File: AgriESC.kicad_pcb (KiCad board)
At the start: 2 copper layers, 94.5 x 53.5 mm, 309 parts, among them J1 SUPPLY, J10 GPIO, J11 USB_OTG, J12 HALL_ENC, J2 PH_A, J3 PH_B, J4 PH_C, J6 COMM, J7 SERVO, J8 CAN, J9 SWD, SW1 SW_SPDT, U1 FDMS7698, U10 STM32F405RGT6, U11 DRV8303, U12 TJA1051TK-3, U13 LMR16006YQ, U14 MCP1700-3302E_SOT23, U15 MCP1700-3302E_SOT23, U2 FDMS7698, U3 FDMS7698, U4 FDMS7698, U5 FDMS7698, U6 FDMS7698, U7 MAX9920, U8 MAX9920, U9 MAX9920, Y1 8M Resonator

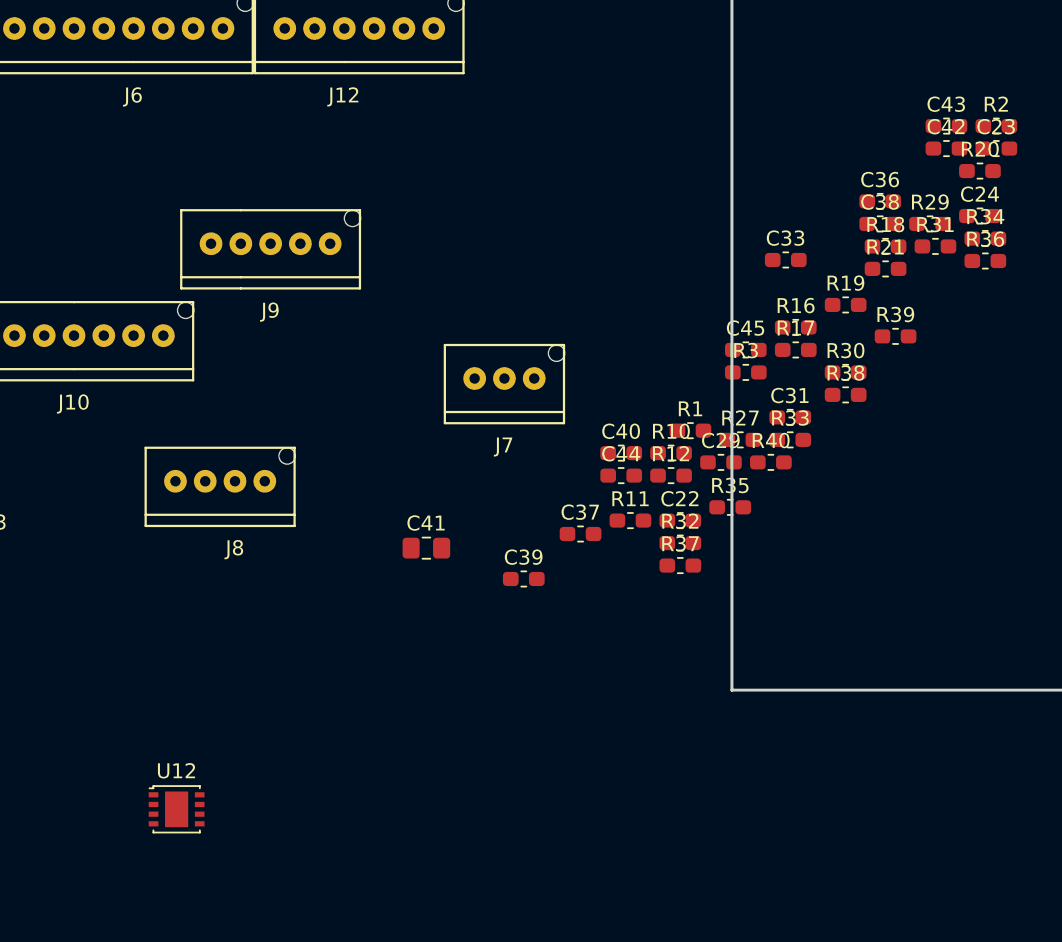
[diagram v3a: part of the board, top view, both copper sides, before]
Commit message: Added CAN wiring
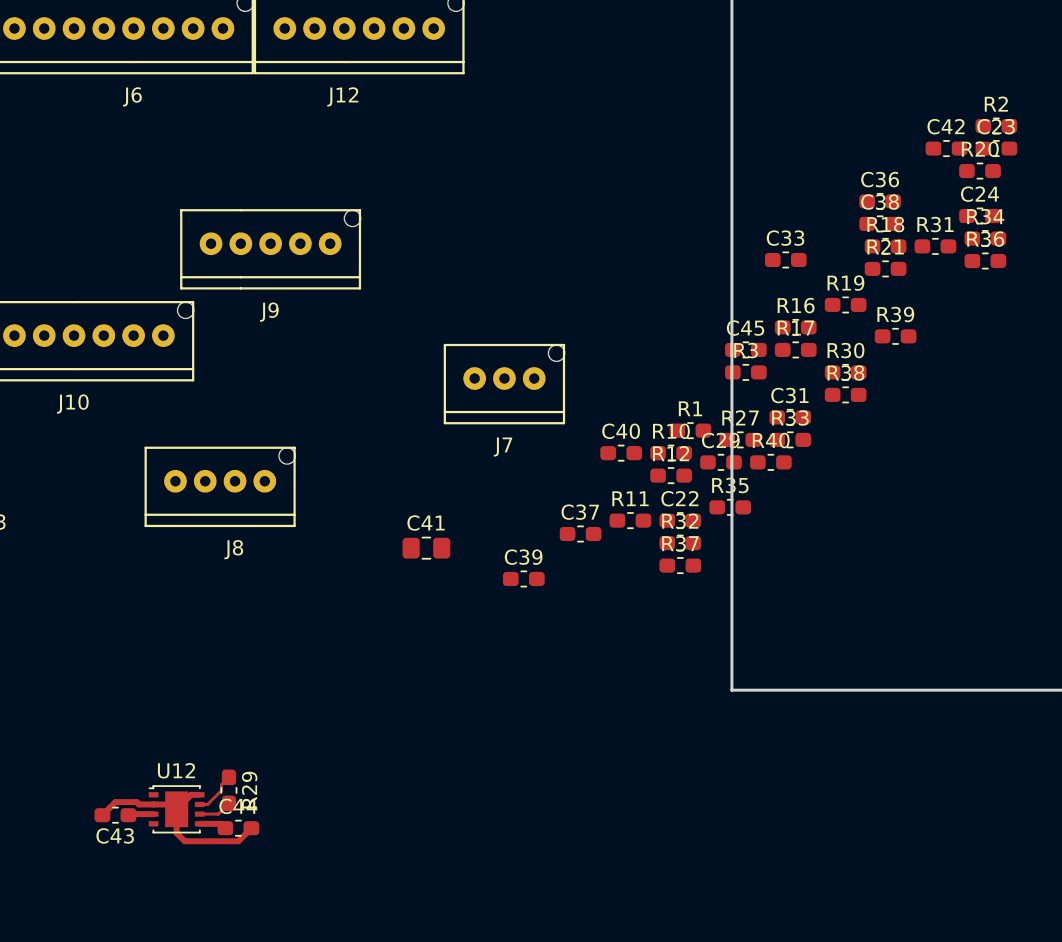
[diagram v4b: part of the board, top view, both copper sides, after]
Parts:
- moved C43 72.5 mm to (14.6, 63.9), turned to 180 degrees
- moved R29 60.5 mm to (22.2, 62.2), turned to 270 degrees
- moved C44 34.9 mm to (22.9, 64.8)
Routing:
- net SL_A: track 198.0 -> 212.7 mm
- net CANH: track 0.00 -> 2.94 mm
- net CANL: track 0.00 -> 2.26 mm
- net VCC: track 2.21 -> 4.05 mm
- net +5V: track 29.0 -> 30.7 mm
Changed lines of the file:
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@@
     (thickness 1.6)
     (drawings 4)
-    (tracks 373)
+    (tracks 396)
     (zones 0)
     (modules 309)
@@
   )
   (setup
-    (last_trace_width 0.2)
+    (last_trace_width 0.4)
     (user_trace_width 0.2)
     (user_trace_width 0.3)
@@
   )
   (module Capacitor_SMD:C_0603_1608Metric_Pad1.05x0.95mm_HandSolder (layer F.Cu)
-    (at 70.405001 17.625001)
+    (at 14.605 63.895 180)
     (descr "Capacitor SMD 0603 (1608 Metric), square (rectangular) end terminal, IPC_7351 nominal with elongated pad for handsoldering. (Body size source: http://www.tortai-tech.com/upload/download/2011102023233369053.pdf), generated with kicad-footprint-generator")
     (tags "capacitor handsolder")
     (attr smd)
-    (fp_text reference C43 (at 0 -1.43) (layer F.SilkS)
+    (fp_text reference C43 (at 0 -1.43 180) (layer F.SilkS)
       (effects (font (size 1 1) (thickness 0.15)))
     )
-    (fp_text value 2u2_5V (at 0 1.43) (layer F.Fab)
+    (fp_text value 2u2_5V (at 0 1.43 180) (layer F.Fab)
       (effects (font (size 1 1) (thickness 0.15)))
     )
@@
     (fp_line (start 1.65 -0.73) (end 1.65 0.73) (layer F.CrtYd) (width 0.05))
     (fp_line (start 1.65 0.73) (end -1.65 0.73) (layer F.CrtYd) (width 0.05))
-    (fp_text user %R (at 0 0) (layer F.Fab)
+    (fp_text user %R (at 0 0 180) (layer F.Fab)
       (effects (font (size 0.4 0.4) (thickness 0.06)))
     )
-    (pad 1 smd roundrect (at -0.875 0) (size 1.05 0.95) (layers F.Cu F.Paste F.Mask) (roundrect_rratio 0.25)
+    (pad 1 smd roundrect (at -0.875 0 180) (size 1.05 0.95) (layers F.Cu F.Paste F.Mask) (roundrect_rratio 0.25)
       (net 23 +5V))
-    (pad 2 smd roundrect (at 0.875 0) (size 1.05 0.95) (layers F.Cu F.Paste F.Mask) (roundrect_rratio 0.25)
+    (pad 2 smd roundrect (at 0.875 0 180) (size 1.05 0.95) (layers F.Cu F.Paste F.Mask) (roundrect_rratio 0.25)
       (net 1 SL_A))
     (model ${KISYS3DMOD}/Capacitor_SMD.3dshapes/C_0603_1608Metric.wrl
@@
   )
   (module Capacitor_SMD:C_0603_1608Metric_Pad1.05x0.95mm_HandSolder (layer F.Cu)
-    (at 48.565001 41.095001)
+    (at 22.86 64.77)
     (descr "Capacitor SMD 0603 (1608 Metric), square (rectangular) end terminal, IPC_7351 nominal with elongated pad for handsoldering. (Body size source: http://www.tortai-tech.com/upload/download/2011102023233369053.pdf), generated with kicad-footprint-generator")
     (tags "capacitor handsolder")
@@
   )
   (module Resistor_SMD:R_0603_1608Metric_Pad1.05x0.95mm_HandSolder (layer F.Cu)
-    (at 69.305001 24.195001)
+    (at 22.225 62.23 270)
     (descr "Resistor SMD 0603 (1608 Metric), square (rectangular) end terminal, IPC_7351 nominal with elongated pad for handsoldering. (Body size source: http://www.tortai-tech.com/upload/download/2011102023233369053.pdf), generated with kicad-footprint-generator")
     (tags "resistor handsolder")
     (attr smd)
-    (fp_text reference R29 (at 0 -1.43) (layer F.SilkS)
+    (fp_text reference R29 (at 0 -1.43 270) (layer F.SilkS)
       (effects (font (size 1 1) (thickness 0.15)))
     )
-    (fp_text value 220R (at 0 1.43) (layer F.Fab)
+    (fp_text value 220R (at 0 1.43 270) (layer F.Fab)
       (effects (font (size 1 1) (thickness 0.15)))
     )
-    (fp_text user %R (at 0 0) (layer F.Fab)
+    (fp_text user %R (at 0 0 270) (layer F.Fab)
       (effects (font (size 0.4 0.4) (thickness 0.06)))
     )
@@
     (fp_line (start -0.8 -0.4) (end 0.8 -0.4) (layer F.Fab) (width 0.1))
     (fp_line (start -0.8 0.4) (end -0.8 -0.4) (layer F.Fab) (width 0.1))
-    (pad 2 smd roundrect (at 0.875 0) (size 1.05 0.95) (layers F.Cu F.Paste F.Mask) (roundrect_rratio 0.25)
+    (pad 2 smd roundrect (at 0.875 0 270) (size 1.05 0.95) (layers F.Cu F.Paste F.Mask) (roundrect_rratio 0.25)
       (net 42 CANL))
-    (pad 1 smd roundrect (at -0.875 0) (size 1.05 0.95) (layers F.Cu F.Paste F.Mask) (roundrect_rratio 0.25)
+    (pad 1 smd roundrect (at -0.875 0 270) (size 1.05 0.95) (layers F.Cu F.Paste F.Mask) (roundrect_rratio 0.25)
       (net 41 CANH))
     (model ${KISYS3DMOD}/Resistor_SMD.3dshapes/R_0603_1608Metric.wrl
@@
   (segment (start 55.245 91.44) (end 58.42 94.615) (width 0.2) (layer B.Cu) (net 1))
   (segment (start 55.245 87.63) (end 55.245 91.44) (width 0.2) (layer B.Cu) (net 1))
+  (segment (start 19.690001 62.525) (end 18.715001 63.5) (width 0.4) (layer F.Cu) (net 1))
+  (segment (start 20.265001 62.525) (end 19.690001 62.525) (width 0.4) (layer F.Cu) (net 1))
+  (segment (start 18.390001 63.175) (end 18.715001 63.5) (width 0.4) (layer F.Cu) (net 1))
+  (segment (start 17.165001 63.175) (end 18.390001 63.175) (width 0.4) (layer F.Cu) (net 1))
+  (segment (start 14.229072 63.395928) (end 13.73 63.895) (width 0.4) (layer F.Cu) (net 1))
+  (segment (start 14.60501 63.01999) (end 14.229072 63.395928) (width 0.4) (layer F.Cu) (net 1))
+  (segment (start 16.031566 63.01999) (end 14.60501 63.01999) (width 0.4) (layer F.Cu) (net 1))
+  (segment (start 16.186576 63.175) (end 16.031566 63.01999) (width 0.4) (layer F.Cu) (net 1))
+  (segment (start 17.165001 63.175) (end 16.186576 63.175) (width 0.4) (layer F.Cu) (net 1))
+  (segment (start 18.715001 65.1) (end 18.715001 63.5) (width 0.4) (layer F.Cu) (net 1))
+  (segment (start 22.85999 65.64501) (end 19.260011 65.64501) (width 0.4) (layer F.Cu) (net 1))
+  (segment (start 19.260011 65.64501) (end 18.715001 65.1) (width 0.4) (layer F.Cu) (net 1))
+  (segment (start 23.735 64.77) (end 22.85999 65.64501) (width 0.4) (layer F.Cu) (net 1))
   (segment (start 114.775 22.975) (end 114.75 23) (width 0.25) (layer F.Cu) (net 2))
   (segment (start 114.775 21) (end 114.775 22.975) (width 0.25) (layer F.Cu) (net 2))
@@
   (segment (start 58.615 -8.015) (end 58.69 -7.94) (width 0.4) (layer F.Cu) (net 4))
   (segment (start 56.515 -8.015) (end 58.615 -8.015) (width 0.4) (layer F.Cu) (net 4))
+  (segment (start 21.69 64.475) (end 21.985 64.77) (width 0.4) (layer F.Cu) (net 4))
+  (segment (start 20.265001 64.475) (end 21.69 64.475) (width 0.4) (layer F.Cu) (net 4))
   (segment (start 119.217 34.5) (end 119.25 34.5) (width 0.2) (layer F.Cu) (net 12))
   (segment (start 117.405 36.312) (end 119.217 34.5) (width 0.2) (layer F.Cu) (net 12))
@@
   (segment (start 61.99 -8.89) (end 62.865 -8.015) (width 0.4) (layer F.Cu) (net 23))
   (segment (start 60.69 -8.89) (end 61.99 -8.89) (width 0.4) (layer F.Cu) (net 23))
+  (segment (start 15.55 63.825) (end 15.48 63.895) (width 0.4) (layer F.Cu) (net 23))
+  (segment (start 17.165001 63.825) (end 15.55 63.825) (width 0.4) (layer F.Cu) (net 23))
   (segment (start 58.07 88.73) (end 59.17 87.63) (width 0.4) (layer F.Cu) (net 25))
   (segment (start 56.195 88.73) (end 58.07 88.73) (width 0.4) (layer F.Cu) (net 25))
@@
   (segment (start 145.75 39.9875) (end 146.75 40.9875) (width 0.2) (layer F.Cu) (net 34))
   (segment (start 145.75 39.75) (end 145.75 39.9875) (width 0.2) (layer F.Cu) (net 34))
+  (segment (start 21.725928 61.854072) (end 22.225 61.355) (width 0.2) (layer F.Cu) (net 41))
+  (segment (start 21.725928 62.239073) (end 21.725928 61.854072) (width 0.2) (layer F.Cu) (net 41))
+  (segment (start 20.790001 63.175) (end 21.725928 62.239073) (width 0.2) (layer F.Cu) (net 41))
+  (segment (start 20.265001 63.175) (end 20.790001 63.175) (width 0.2) (layer F.Cu) (net 41))
+  (segment (start 21.505 63.825) (end 22.225 63.105) (width 0.2) (layer F.Cu) (net 42))
+  (segment (start 20.265001 63.825) (end 21.505 63.825) (width 0.2) (layer F.Cu) (net 42))
   (segment (start 74.295 -26.275) (end 73.025 -25.005) (width 0.2) (layer F.Cu) (net 49))
   (segment (start 74.295 -27.305) (end 74.295 -26.275) (width 0.2) (layer F.Cu) (net 49))

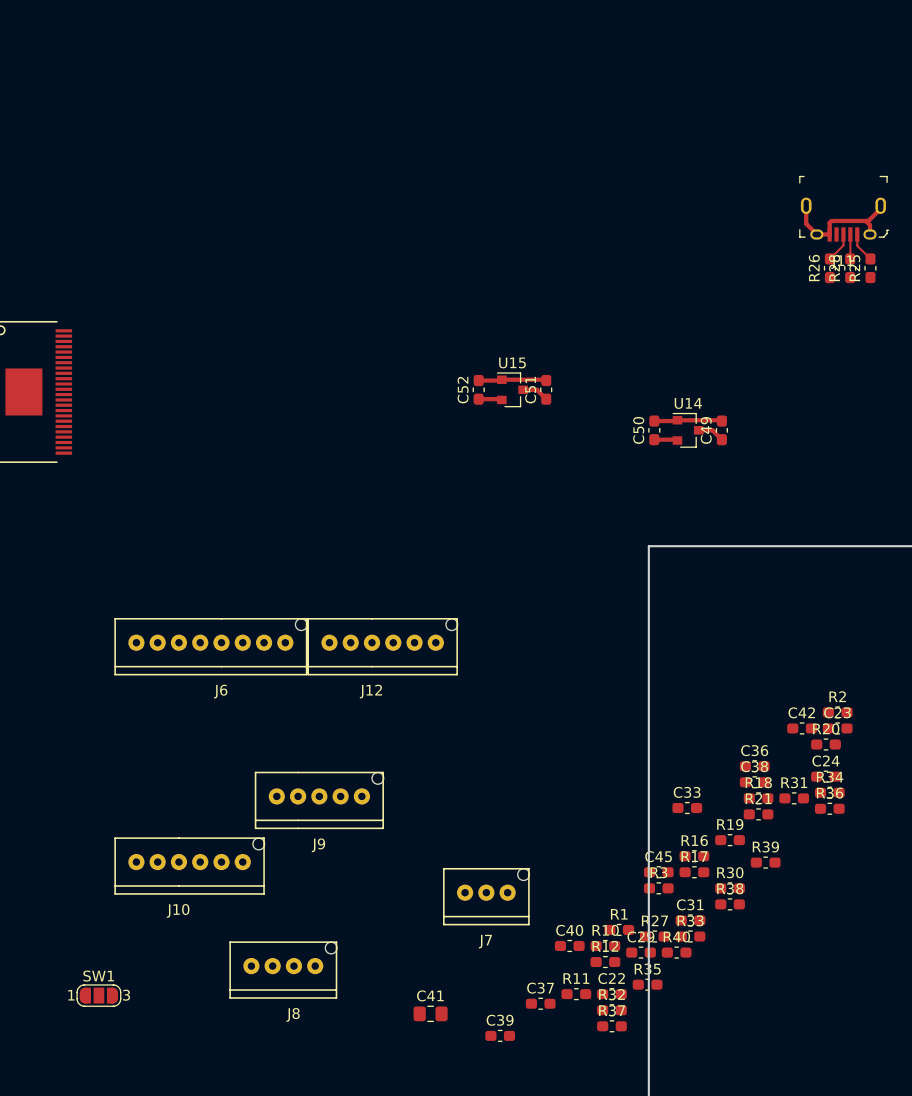
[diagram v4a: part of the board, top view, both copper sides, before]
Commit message: Arranged hall sensors
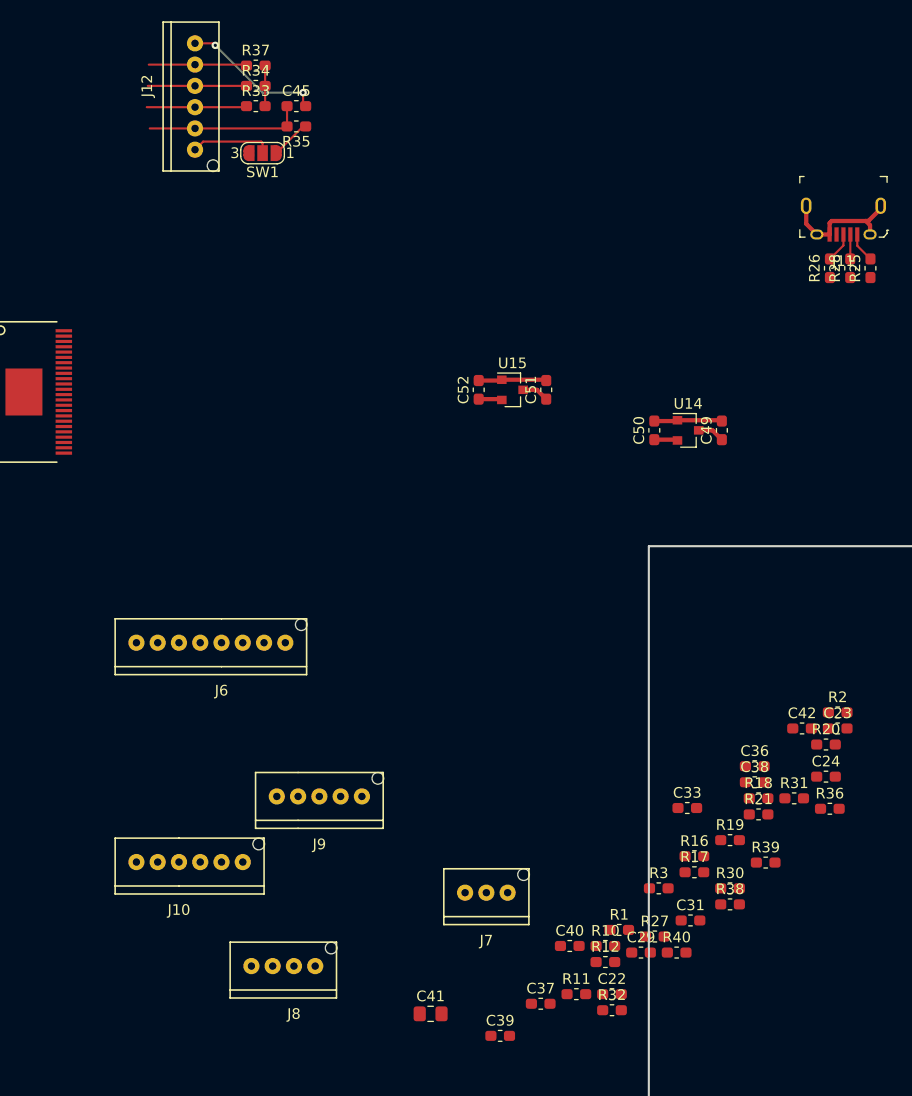
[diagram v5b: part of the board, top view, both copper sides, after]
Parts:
- moved R37 96.3 mm to (19.1, -43.2)
- moved R33 88.1 mm to (19.1, -39.4)
- moved R35 87.2 mm to (22.9, -37.5), turned to 180 degrees
- moved R34 85.6 mm to (19.1, -41.3)
- moved SW1 80.7 mm to (19.7, -35.0), turned to 180 degrees
- moved C45 79.7 mm to (22.9, -39.4)
- moved J12 54.9 mm to (13.3, -41.3), turned to 270 degrees
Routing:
- net TEMP_MOTOR: track 0.00 -> 14.9 mm
- net SL_A: track 212.7 -> 226.1 mm, vias 10 -> 12
- net Net-(J12-Pad6): track 0.00 -> 11.8 mm
- net HALL_1: track 0.00 -> 9.42 mm
- net HALL_2: track 0.00 -> 9.29 mm
- net HALL_3: track 0.00 -> 9.23 mm
- net VCC: track 4.05 -> 7.84 mm

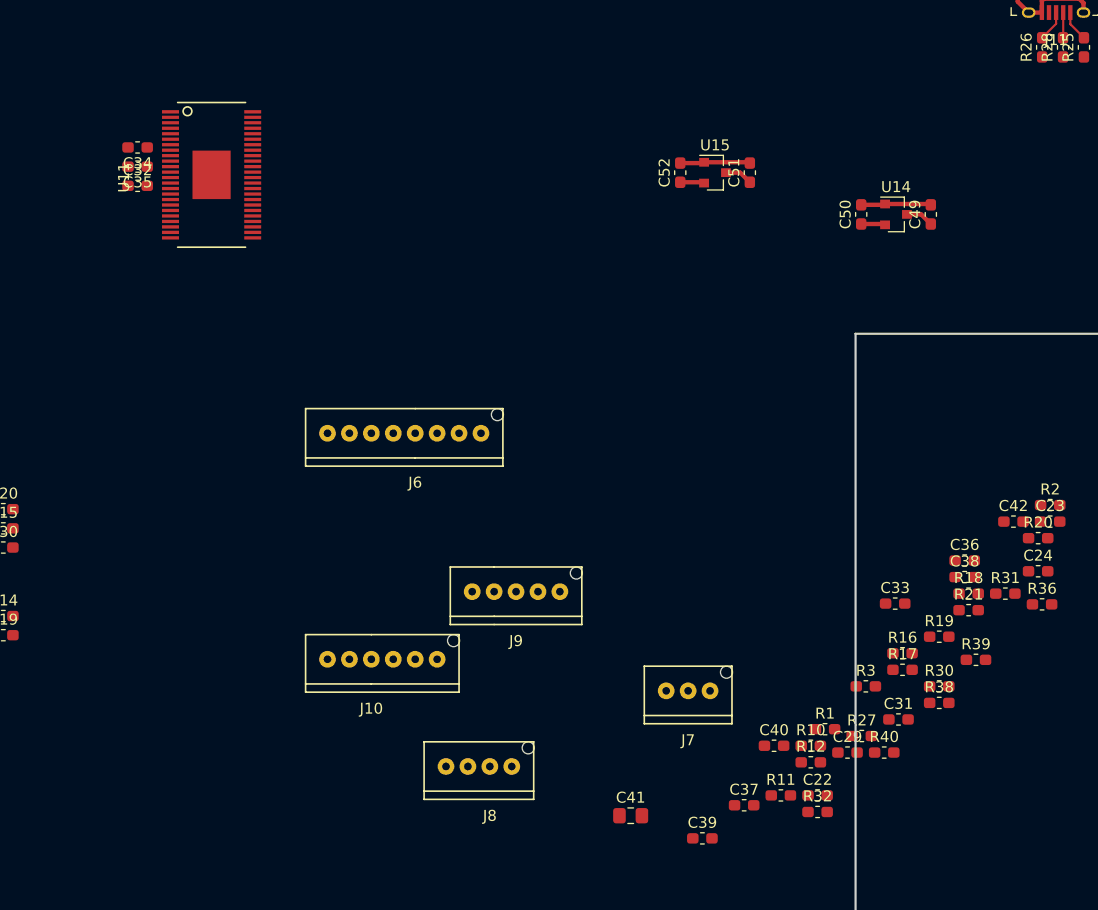
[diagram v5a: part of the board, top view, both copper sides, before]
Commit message: Wiring for motor driver
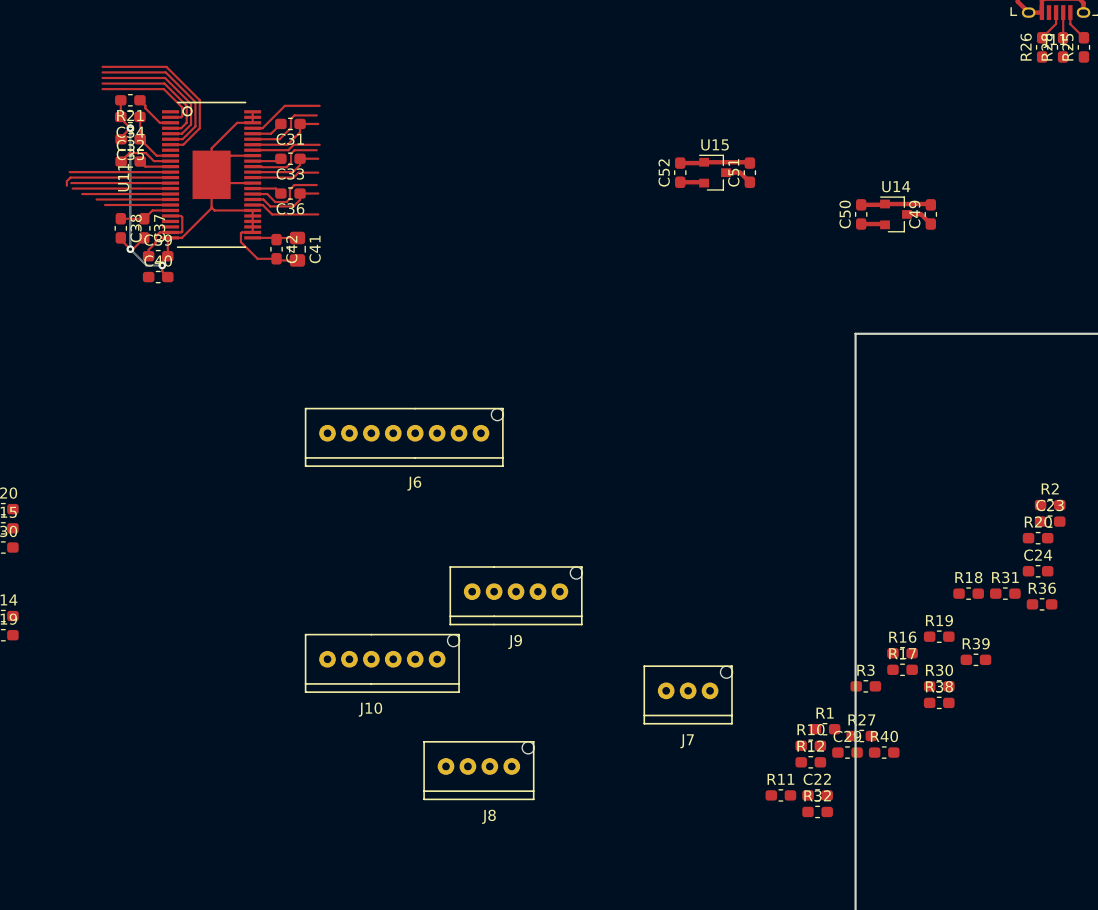
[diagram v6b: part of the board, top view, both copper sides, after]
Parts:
- moved R21 89.5 mm to (-10.2, -19.3), turned to 180 degrees
- moved C38 83.3 mm to (-11.0, -7.62), turned to 270 degrees
- moved C31 77.6 mm to (4.45, -17.1), turned to 180 degrees
- moved C37 75.9 mm to (-8.89, -7.62), turned to 270 degrees
- moved C39 72.7 mm to (-7.62, -5.08)
- moved C42 71.7 mm to (3.17, -5.71), turned to 270 degrees
- moved C40 70.6 mm to (-7.62, -3.17)
- moved C36 70.0 mm to (4.45, -10.8), turned to 180 degrees
- moved C33 68.5 mm to (4.45, -14.0), turned to 180 degrees
- moved C41 60.0 mm to (5.08, -5.71), turned to 270 degrees
- moved C34 2.86 mm to (-10.2, -17.8)
- moved C35 2.58 mm to (-10.1, -15.7)
- moved C32 2.31 mm to (-10.1, -13.7)
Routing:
- net SL_A: track 226.1 -> 290.5 mm, vias 12 -> 15
- net SCLK: track 0.00 -> 16.0 mm
- net SDO: track 0.00 -> 14.6 mm
- net SDI: track 0.00 -> 13.2 mm
- net CS: track 0.00 -> 11.8 mm
- net H1: track 0.00 -> 10.00 mm
- net FAULT: track 0.00 -> 9.88 mm
- net EN_GATE: track 0.00 -> 9.20 mm
- net INL_A: track 0.00 -> 9.05 mm
- net H2: track 0.00 -> 8.92 mm
- net INL_B: track 0.00 -> 8.06 mm
- net GH_C: track 0.00 -> 7.27 mm
- net GH_A: track 0.00 -> 7.22 mm
- net SH_A: track 30.1 -> 37.3 mm
- net Net-(C39-Pad1): track 0.00 -> 7.09 mm
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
